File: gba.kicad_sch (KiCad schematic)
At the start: 29 parts, among them IC1 STM32MP157AAB3, IC7 S40FC004C1B2C00000, IC9 NXS0506UPZ, J2 Conn_01x02, J3 MEM2075-00-140-01-A, SW1 SW_MEC_5G, SW2 SW_MEC_5G

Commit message: Add SDCard connection to mpu
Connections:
- net SD_CLK: now also IC1.C10 (PC12)
- net SD_CMD: now also IC1.B10 (PD2)
- net SD_DAT0: now also IC1.C11 (PC8)
- net SD_DAT1: now also IC1.A10 (PC9)
- net SD_DAT2: now also IC1.D11 (PC10)
- net SD_DAT3: now also IC1.A11 (PC11)
- net VOUT_LDO5 renamed LDO5_2V9
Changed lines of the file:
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@@
+    (stroke (width 0) (type default))
+  )
+  (wire (pts (xy 74.93 175.26) (xy 83.82 175.26))
     (stroke (width 0) (type default))
   )
@@
     (stroke (width 0) (type default))
   )
+  (wire (pts (xy 74.93 172.72) (xy 83.82 172.72))
+    (stroke (width 0) (type default))
+  )
   (wire (pts (xy 274.32 82.55) (xy 271.78 82.55))
     (stroke (width 0) (type default))
@@
     (stroke (width 0) (type default))
   )
+  (wire (pts (xy 74.93 93.98) (xy 83.82 93.98))
+    (stroke (width 0) (type default))
+  )
   (wire (pts (xy 381 62.23) (xy 384.81 62.23))
     (stroke (width 0) (type default))
@@
     (stroke (width 0) (type default))
   )
+  (wire (pts (xy 74.93 96.52) (xy 83.82 96.52))
+    (stroke (width 0) (type default))
+  )
   (wire (pts (xy 246.38 49.53) (xy 250.19 49.53))
     (stroke (width 0) (type default))
@@
     (stroke (width 0) (type default))
   )
+  (wire (pts (xy 76.2 132.08) (xy 83.82 132.08))
+    (stroke (width 0) (type default))
+  )
   (wire (pts (xy 332.74 128.27) (xy 332.74 130.81))
+    (stroke (width 0) (type default))
+  )
+  (wire (pts (xy 76.2 198.12) (xy 83.82 198.12))
     (stroke (width 0) (type default))
   )
@@
     )
   )
+  (global_label "SD_DAT1" (shape input) (at 74.93 93.98 180) (fields_autoplaced)
+    (effects (font (size 1.27 1.27)) (justify right))
+    (property "Intersheetrefs" "${INTERSHEET_REFS}" (at 64.0414 93.98 0)
+      (effects (font (size 1.27 1.27)) (justify right) hide)
+    )
+  )
   (global_label "SD_DAT1" (shape input) (at 345.44 52.07 180) (fields_autoplaced)
     (effects (font (size 1.27 1.27)) (justify right))
@@
     )
   )
+  (global_label "SD_CLK" (shape input) (at 74.93 172.72 180) (fields_autoplaced)
+    (effects (font (size 1.27 1.27)) (justify right))
+    (property "Intersheetrefs" "${INTERSHEET_REFS}" (at 65.009 172.72 0)
+      (effects (font (size 1.27 1.27)) (justify right) hide)
+    )
+  )
   (global_label "UART4_RX" (shape input) (at 246.38 46.99 180) (fields_autoplaced)
     (effects (font (size 1.27 1.27)) (justify right))
@@
     )
   )
+  (global_label "SD_CMD" (shape input) (at 76.2 132.08 180) (fields_autoplaced)
+    (effects (font (size 1.27 1.27)) (justify right))
+    (property "Intersheetrefs" "${INTERSHEET_REFS}" (at 65.8557 132.08 0)
+      (effects (font (size 1.27 1.27)) (justify right) hide)
+    )
+  )
   (global_label "DDR_BA2" (shape input) (at 146.05 38.1 0) (fields_autoplaced)
     (effects (font (size 1.27 1.27)) (justify left))
@@
     )
   )
-  (global_label "VOUT_LDO5" (shape input) (at 394.97 114.3 90) (fields_autoplaced)
+  (global_label "LDO5_2V9" (shape input) (at 394.97 114.3 90) (fields_autoplaced)
     (effects (font (size 1.27 1.27)) (justify left))
     (property "Intersheetrefs" "${INTERSHEET_REFS}" (at 394.97 100.8713 90)
@@
     (effects (font (size 1.27 1.27)) (justify right))
     (property "Intersheetrefs" "${INTERSHEET_REFS}" (at 327.3549 134.62 0)
+      (effects (font (size 1.27 1.27)) (justify right) hide)
+    )
+  )
+  (global_label "SD_DAT2" (shape input) (at 76.2 198.12 180) (fields_autoplaced)
+    (effects (font (size 1.27 1.27)) (justify right))
+    (property "Intersheetrefs" "${INTERSHEET_REFS}" (at 65.3114 198.12 0)
       (effects (font (size 1.27 1.27)) (justify right) hide)
     )
@@
     )
   )
+  (global_label "SD_DAT0" (shape input) (at 74.93 175.26 180) (fields_autoplaced)
+    (effects (font (size 1.27 1.27)) (justify right))
+    (property "Intersheetrefs" "${INTERSHEET_REFS}" (at 64.0414 175.26 0)
+      (effects (font (size 1.27 1.27)) (justify right) hide)
+    )
+  )
   (global_label "BUCK4_1V8" (shape input) (at 271.78 72.39 90) (fields_autoplaced)
     (effects (font (size 1.27 1.27)) (justify left))
@@
     )
   )
-  (global_label "VOUT_LDO5" (shape input) (at 360.68 105.41 0) (fields_autoplaced)
+  (global_label "LDO5_2V9" (shape input) (at 360.68 105.41 0) (fields_autoplaced)
     (effects (font (size 1.27 1.27)) (justify left))
     (property "Intersheetrefs" "${INTERSHEET_REFS}" (at 374.1087 105.41 0)
@@
     )
   )
-  (global_label "VOUT_LDO5" (shape input) (at 317.5 104.14 0) (fields_autoplaced)
+  (global_label "LDO5_2V9" (shape input) (at 317.5 104.14 0) (fields_autoplaced)
     (effects (font (size 1.27 1.27)) (justify left))
     (property "Intersheetrefs" "${INTERSHEET_REFS}" (at 330.9287 104.14 0)
@@
     )
   )
+  (global_label "SD_DAT3" (shape input) (at 74.93 96.52 180) (fields_autoplaced)
+    (effects (font (size 1.27 1.27)) (justify right))
+    (property "Intersheetrefs" "${INTERSHEET_REFS}" (at 64.0414 96.52 0)
+      (effects (font (size 1.27 1.27)) (justify right) hide)
+    )
+  )

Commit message: Added nRF Bluetooth Chip
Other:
- added sheet Communication (communication.kicad_sch)
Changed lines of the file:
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@@
+    )
+  )
+  (sheet (at 299.72 203.2) (size 25.4 12.7) (fields_autoplaced)
+    (stroke (width 0.1524) (type solid))
+    (fill (color 0 0 0 0.0000))
+    (property "Sheetname" "Communication" (at 299.72 202.4884 0)
+      (effects (font (size 1.27 1.27)) (justify left bottom))
+    )
+    (property "Sheetfile" "communication.kicad_sch" (at 299.72 216.4846 0)
+      (effects (font (size 1.27 1.27)) (justify left top))
+    )
+    (instances
+      (project "gba"
+        (path "/017c50c6-333c-4d31-ad5a-278994a09b14" (page "4"))
+      )
     )
   )

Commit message: added footprint for nRF, changed symbol background color, checked connections
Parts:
- renumbered R to R63
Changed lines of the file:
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@@
   (symbol (lib_id "Device:R_Small") (at 254 77.47 0) (unit 1)
     (in_bom yes) (on_board yes) (dnp no) (fields_autoplaced)
-    (property "Reference" "R" (at 256.54 76.835 0)
+    (property "Reference" "R63" (at 256.54 76.835 0)
       (effects (font (size 1.27 1.27)) (justify left))
     )
@@
       (project "gba"
         (path "/017c50c6-333c-4d31-ad5a-278994a09b14"
-          (reference "R") (unit 1)
+          (reference "R63") (unit 1)
         )
       )

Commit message: added supply to nRF
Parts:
- C27, C28, C66: value 1uF -> 1u
- R56, R57, R58, R59, R60, R61: value 47K -> 47k
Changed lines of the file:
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@@
       (effects (font (size 1.27 1.27)) (justify left))
     )
-    (property "Value" "1uF" (at 346.4941 87.6436 0)
+    (property "Value" "1u" (at 346.4941 87.6436 0)
       (effects (font (size 1.27 1.27)) (justify left))
     )
@@
       (effects (font (size 1.27 1.27)) (justify left))
     )
-    (property "Value" "1uF" (at 397.2941 123.2036 0)
+    (property "Value" "1u" (at 397.2941 123.2036 0)
       (effects (font (size 1.27 1.27)) (justify left))
     )
@@
       (effects (font (size 1.27 1.27)))
     )
-    (property "Value" "47K" (at 330.2 109.22 0)
+    (property "Value" "47k" (at 330.2 109.22 0)
       (effects (font (size 1.27 1.27)))
     )
@@
       (effects (font (size 1.27 1.27)))
     )
-    (property "Value" "47K" (at 354.33 110.49 90)
+    (property "Value" "47k" (at 354.33 110.49 90)
       (effects (font (size 1.27 1.27)))
     )
@@
       (effects (font (size 1.27 1.27)) (justify left))
     )
-    (property "Value" "1uF" (at 394.7541 57.1636 0)
+    (property "Value" "1u" (at 394.7541 57.1636 0)
       (effects (font (size 1.27 1.27)) (justify left))
     )
@@
       (effects (font (size 1.27 1.27)))
     )
-    (property "Value" "47K" (at 360.68 110.49 90)
+    (property "Value" "47k" (at 360.68 110.49 90)
       (effects (font (size 1.27 1.27)))
     )
@@
       (effects (font (size 1.27 1.27)))
     )
-    (property "Value" "47K" (at 347.98 110.49 90)
+    (property "Value" "47k" (at 347.98 110.49 90)
       (effects (font (size 1.27 1.27)))
     )
@@
       (effects (font (size 1.27 1.27)))
     )
-    (property "Value" "47K" (at 341.63 110.49 90)
+    (property "Value" "47k" (at 341.63 110.49 90)
       (effects (font (size 1.27 1.27)))
     )
@@
       (effects (font (size 1.27 1.27)))
     )
-    (property "Value" "47K" (at 337.82 110.49 90)
-      (effects (font (size 1.27 1.27)))
-    )
+    (property "Value" "47k" (at 337.82 110.49 90)
+      (effects (font (size 1.27 1.27)))
+    )

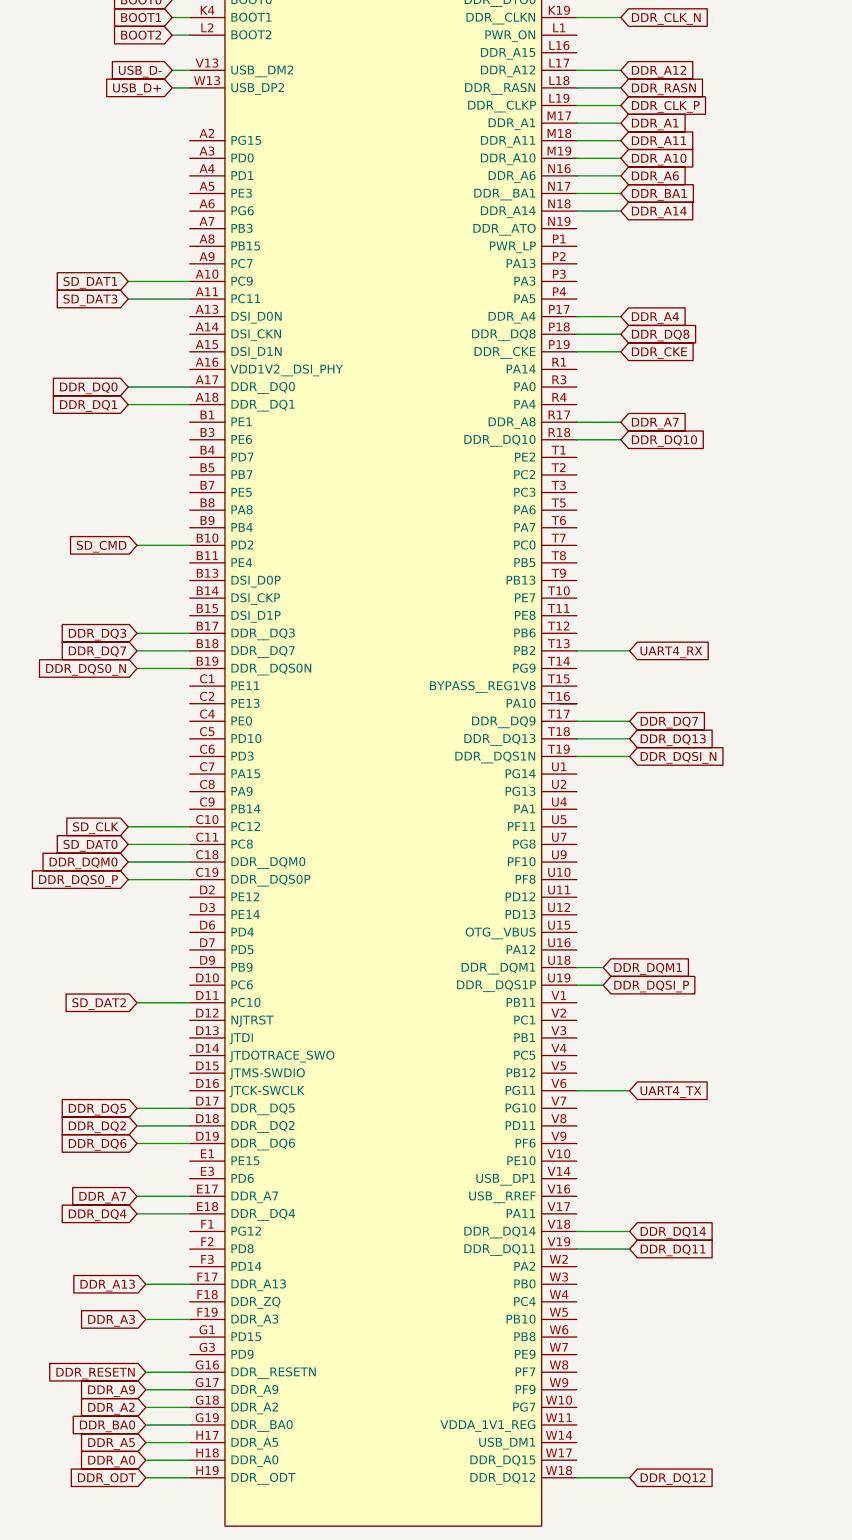
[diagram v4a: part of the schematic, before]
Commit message: added decoupling capacitors to mp1
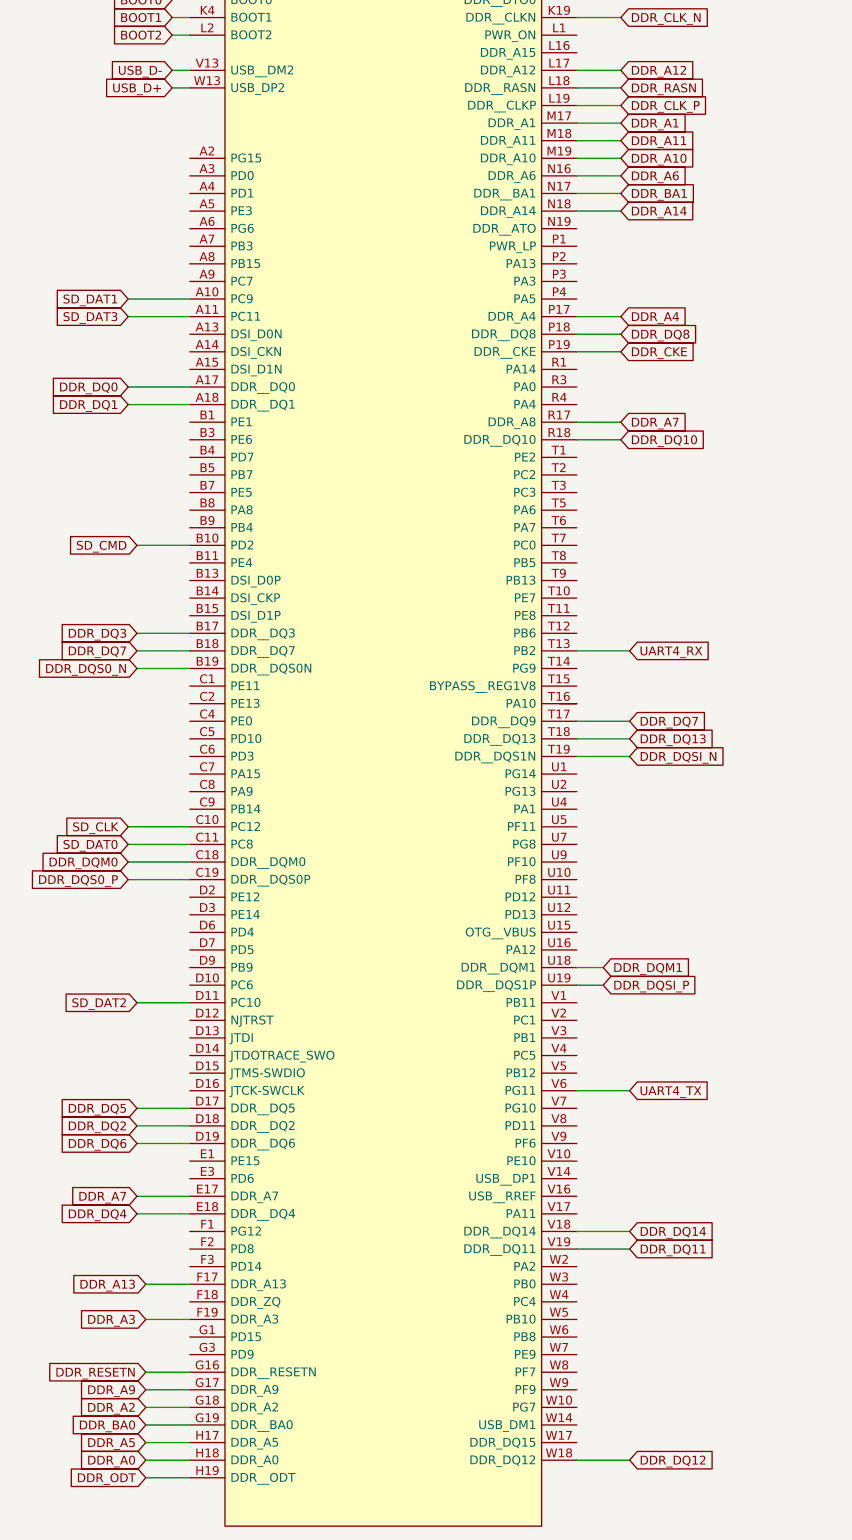
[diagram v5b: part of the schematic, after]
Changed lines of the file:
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@@
     (stroke (width 0) (type default))
   )
-  (wire (pts (xy 74.93 93.98) (xy 83.82 93.98))
+  (wire (pts (xy 74.93 96.52) (xy 83.82 96.52))
     (stroke (width 0) (type default))
   )
@@
     (stroke (width 0) (type default))
   )
-  (wire (pts (xy 74.93 96.52) (xy 83.82 96.52))
+  (wire (pts (xy 74.93 99.06) (xy 83.82 99.06))
     (stroke (width 0) (type default))
   )
@@
     (stroke (width 0) (type default))
   )
-  (wire (pts (xy 139.7 266.7) (xy 147.32 266.7))
+  (wire (pts (xy 139.7 264.16) (xy 147.32 264.16))
     (stroke (width 0) (type default))
   )
@@
     )
   )
-  (global_label "SD_DAT1" (shape input) (at 74.93 93.98 180) (fields_autoplaced)
-    (effects (font (size 1.27 1.27)) (justify right))
-    (property "Intersheetrefs" "${INTERSHEET_REFS}" (at 64.0414 93.98 0)
+  (global_label "SD_DAT1" (shape input) (at 74.93 96.52 180) (fields_autoplaced)
+    (effects (font (size 1.27 1.27)) (justify right))
+    (property "Intersheetrefs" "${INTERSHEET_REFS}" (at 64.0414 96.52 0)
       (effects (font (size 1.27 1.27)) (justify right) hide)
     )
@@
     )
   )
-  (global_label "DDR_DQ12" (shape input) (at 147.32 266.7 0) (fields_autoplaced)
-    (effects (font (size 1.27 1.27)) (justify left))
-    (property "Intersheetrefs" "${INTERSHEET_REFS}" (at 160.0229 266.7 0)
+  (global_label "DDR_DQ12" (shape input) (at 147.32 264.16 0) (fields_autoplaced)
+    (effects (font (size 1.27 1.27)) (justify left))
+    (property "Intersheetrefs" "${INTERSHEET_REFS}" (at 160.0229 264.16 0)
       (effects (font (size 1.27 1.27)) (justify left) hide)
     )
@@
     )
   )
-  (global_label "SD_DAT3" (shape input) (at 74.93 96.52 180) (fields_autoplaced)
-    (effects (font (size 1.27 1.27)) (justify right))
-    (property "Intersheetrefs" "${INTERSHEET_REFS}" (at 64.0414 96.52 0)
+  (global_label "SD_DAT3" (shape input) (at 74.93 99.06 180) (fields_autoplaced)
+    (effects (font (size 1.27 1.27)) (justify right))
+    (property "Intersheetrefs" "${INTERSHEET_REFS}" (at 64.0414 99.06 0)
       (effects (font (size 1.27 1.27)) (justify right) hide)
     )
@@
     (pin "A14")
     (pin "A15")
-    (pin "A16")
     (pin "A17")
     (pin "A18")
@@
     (pin "V9")
     (pin "W10")
-    (pin "W11")
     (pin "W13")
     (pin "W14")
@@
     (pin "A1")
     (pin "A12")
+    (pin "A16")
     (pin "A19")
     (pin "B12")
@@
     (pin "V15")
     (pin "W1")
+    (pin "W11")
     (pin "W12")
     (pin "W15")

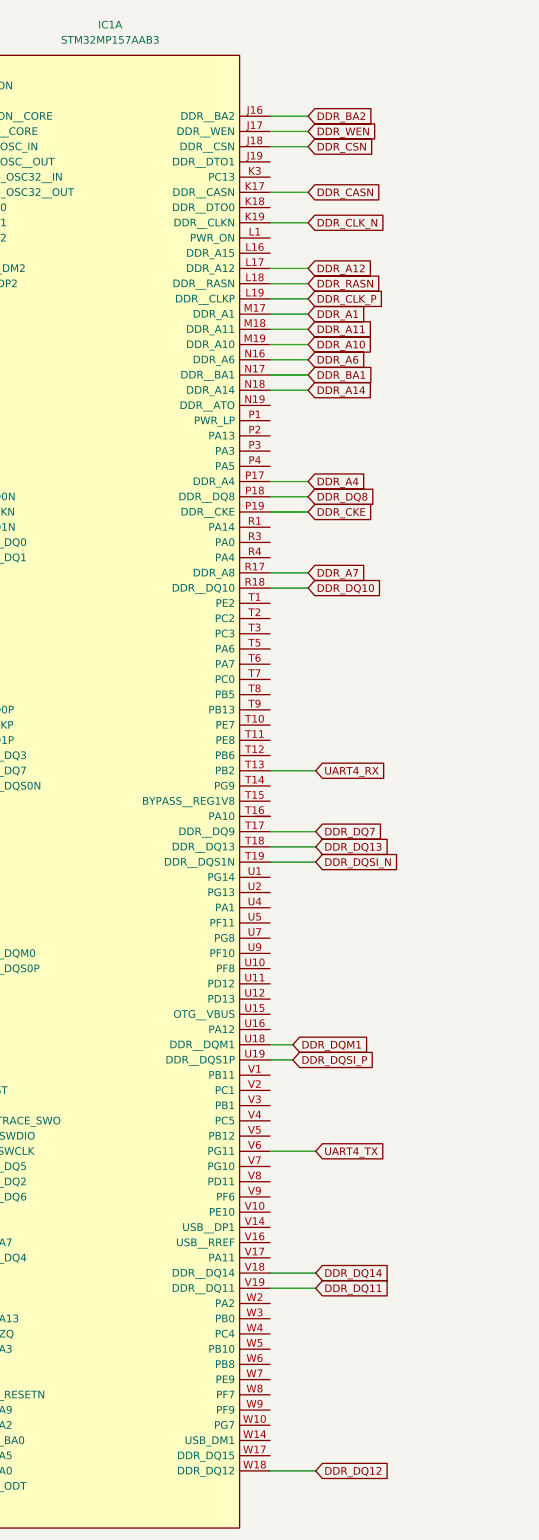
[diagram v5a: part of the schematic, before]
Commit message: changed mp1 symbol and moved BYPASS_REG1V8 signal to supply
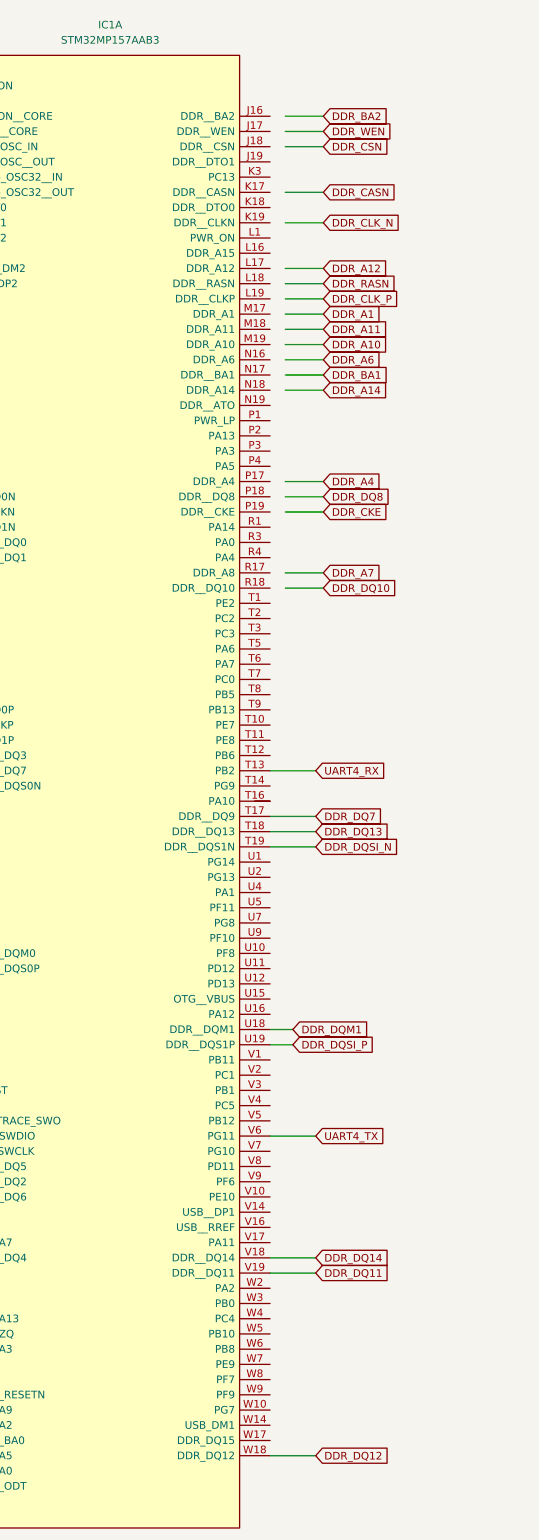
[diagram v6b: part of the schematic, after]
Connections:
- net DDR_A1: no longer IC1.M17 (DDR_A1)
- net DDR_A10: no longer IC1.M19 (DDR_A10)
- net DDR_A11: no longer IC1.M18 (DDR_A11)
- net DDR_A12: no longer IC1.L17 (DDR_A12)
- net DDR_A14: no longer IC1.N18 (DDR_A14)
- net DDR_A4: no longer IC1.P17 (DDR_A4)
- net DDR_A6: no longer IC1.N16 (DDR_A6)
- net DDR_A7: no longer IC1.R17 (DDR_A8)
- net DDR_BA1: no longer IC1.N17 (DDR__BA1)
- net DDR_BA2: no longer IC1.J16 (DDR__BA2)
- net DDR_CASN: no longer IC1.K17 (DDR__CASN)
- net DDR_CKE: no longer IC1.P19 (DDR__CKE)
- net DDR_CLK_N: no longer IC1.K19 (DDR__CLKN)
- net DDR_CLK_P: no longer IC1.L19 (DDR__CLKP)
- net DDR_CSN: no longer IC1.J18 (DDR__CSN)
- net DDR_DQ10: no longer IC1.R18 (DDR__DQ10)
- net DDR_DQ8: no longer IC1.P18 (DDR__DQ8)
- net DDR_RASN: no longer IC1.L18 (DDR__RASN)
- net DDR_WEN: no longer IC1.J17 (DDR__WEN)

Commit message: added I2C4 connection to I2C bus and MP1
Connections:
- net DDR_A1: now also IC1.M17 (DDR_A1)
- net DDR_A10: now also IC1.M19 (DDR_A10)
- net DDR_A11: now also IC1.M18 (DDR_A11)
- net DDR_A12: now also IC1.L17 (DDR_A12)
- net DDR_A14: now also IC1.N18 (DDR_A14)
- net DDR_A4: now also IC1.P17 (DDR_A4)
- net DDR_A6: now also IC1.N16 (DDR_A6)
- net DDR_A7: now also IC1.R17 (DDR_A8)
- net DDR_BA1: now also IC1.N17 (DDR__BA1)
- net DDR_BA2: now also IC1.J16 (DDR__BA2)
- net DDR_CASN: now also IC1.K17 (DDR__CASN)
- net DDR_CKE: now also IC1.P19 (DDR__CKE)
- net DDR_CLK_N: now also IC1.K19 (DDR__CLKN)
- net DDR_CLK_P: now also IC1.L19 (DDR__CLKP)
- net DDR_CSN: now also IC1.J18 (DDR__CSN)
- net DDR_DQ10: now also IC1.R18 (DDR__DQ10)
- net DDR_DQ8: now also IC1.P18 (DDR__DQ8)
- net DDR_RASN: now also IC1.L18 (DDR__RASN)
- net DDR_WEN: now also IC1.J17 (DDR__WEN)
- net SCL: now also IC1.T1 (PE2)
- net SDA: now also IC1.B5 (PB7)
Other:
- note added: "Notes: I2C: AN5031 P. 57: I2C4 is used for communication with PMIC I2C4/I2C6 can be defined as accessible by secure software only (DS P. 52) PE2: I2C4_SCL, PB7: I2C4_SDA (CubeMX & DS p. 93, 96)"
